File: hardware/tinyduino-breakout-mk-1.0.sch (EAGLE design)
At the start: 4 parts, among them J1 DF12-32-DP

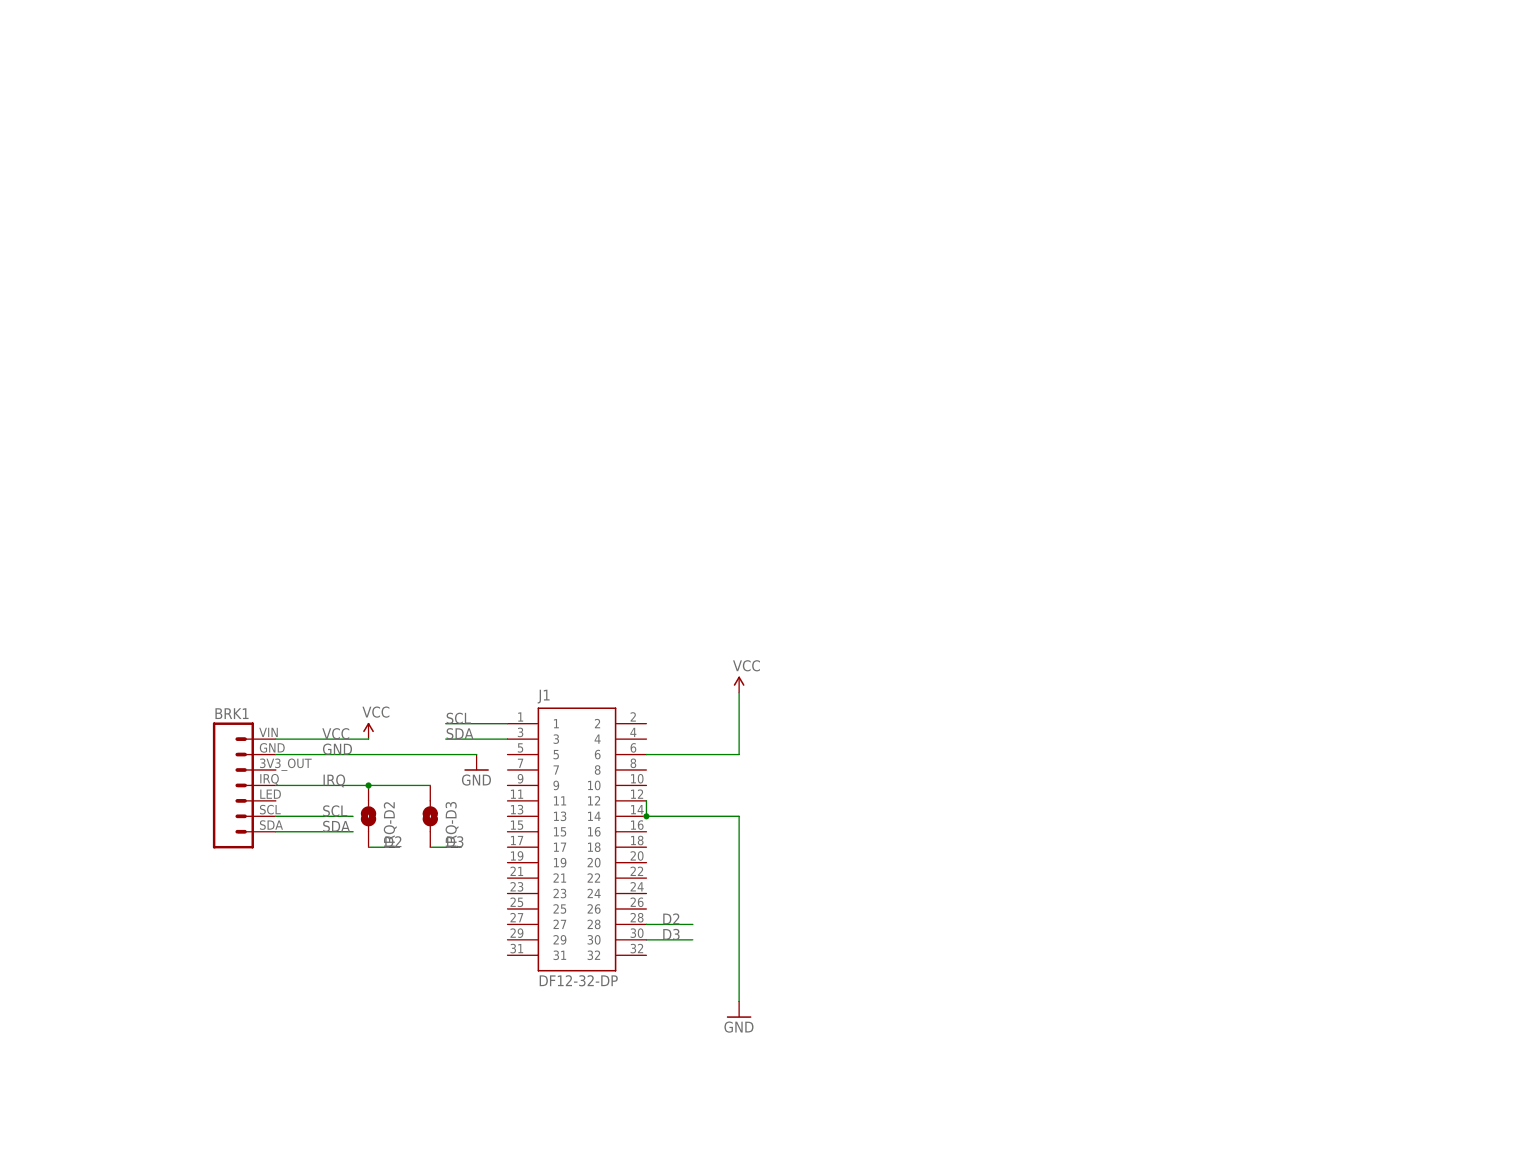
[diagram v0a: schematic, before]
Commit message: adding revsion info to schematic and board
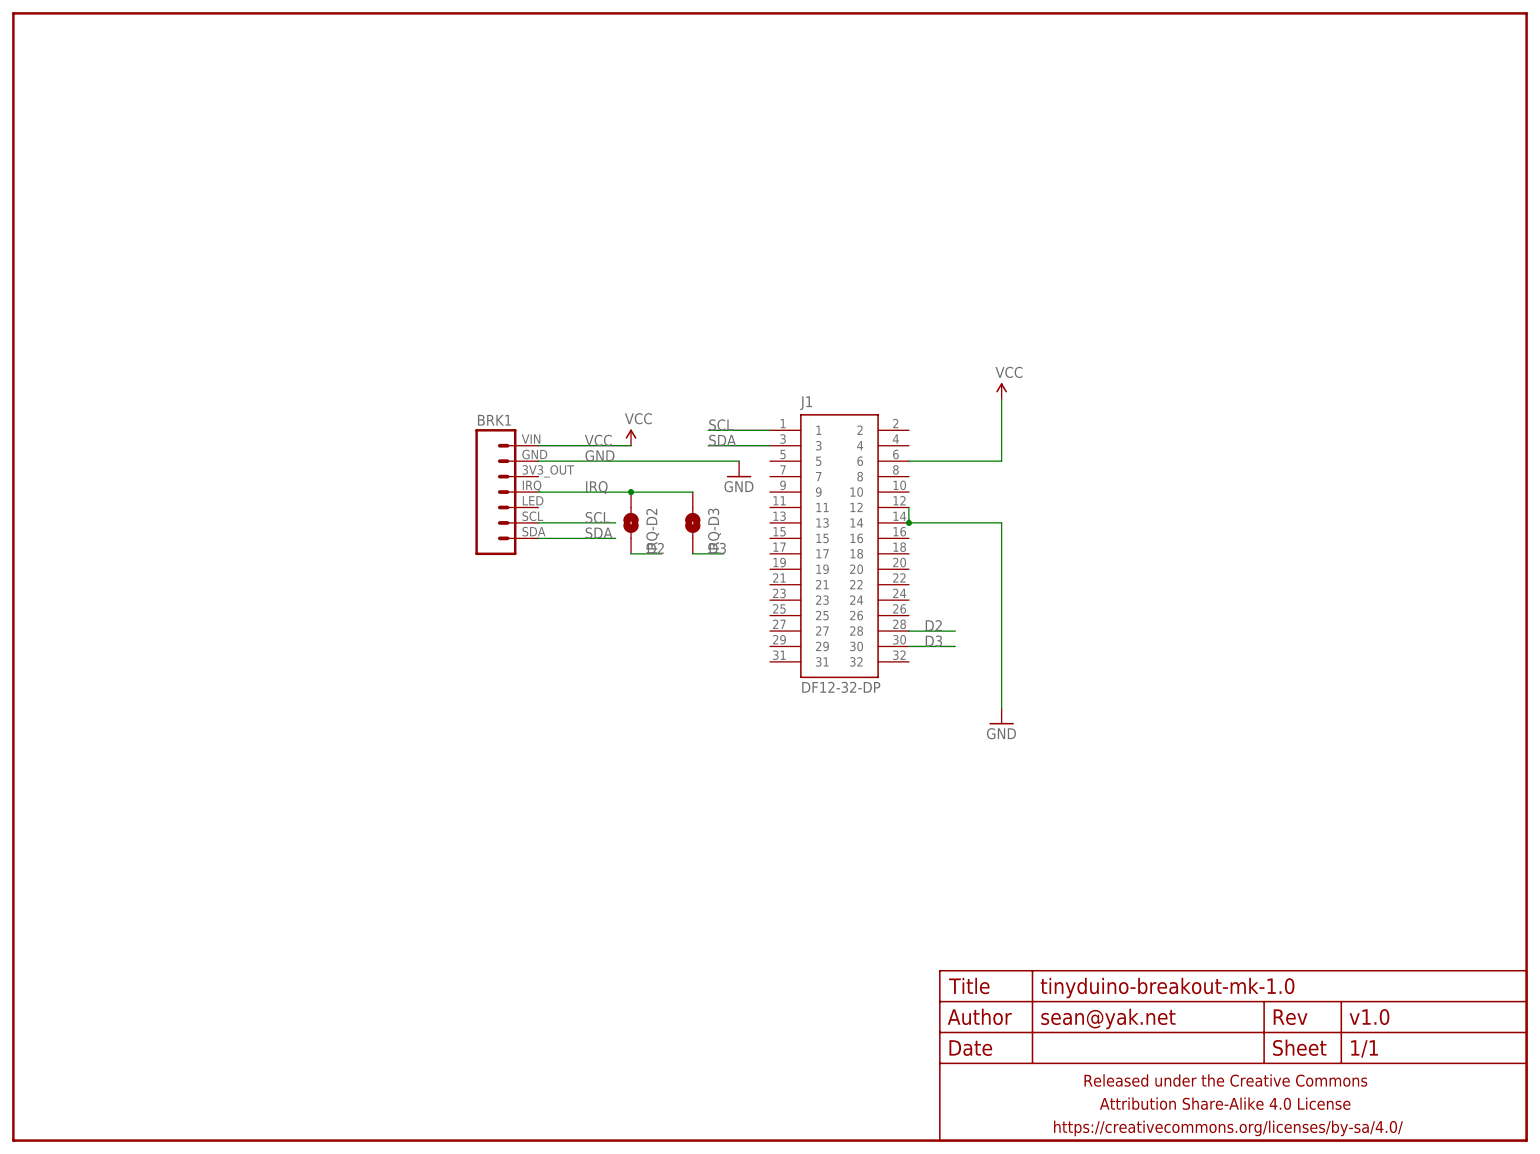
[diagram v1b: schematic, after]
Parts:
- added FRAME1: FRAME-LETTERNO_PACKAGE, A_butts:FRAME-LETTERNO_PACKAGE
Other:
- moved on the sheet: BRK1, IRQ-D2, IRQ-D3, J1
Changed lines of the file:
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@@
 <setting verticaltext="up"/>
 </settings>
-<grid distance="100" unitdist="mil" unit="mil" style="lines" multiple="1" display="yes" altdistance="1" altunitdist="mil" altunit="mil"/>
+<grid distance="100" unitdist="mil" unit="mil" style="lines" multiple="1" display="yes" altdistance="2" altunitdist="mil" altunit="mil"/>
 <layers>
 <layer number="1" name="Top" color="4" fill="1" visible="no" active="no"/>
@@
 <layer number="56" name="wert" color="7" fill="1" visible="no" active="no"/>
 <layer number="57" name="tCAD" color="7" fill="1" visible="no" active="no"/>
+<layer number="90" name="Modules" color="5" fill="1" visible="yes" active="yes"/>
 <layer number="91" name="Nets" color="2" fill="1" visible="yes" active="yes"/>
 <layer number="92" name="Busses" color="1" fill="1" visible="yes" active="yes"/>
@@
 <layer number="223" name="223bmp" color="24" fill="1" visible="yes" active="yes"/>
 <layer number="224" name="224bmp" color="25" fill="1" visible="yes" active="yes"/>
+<layer number="225" name="225bmp" color="7" fill="1" visible="yes" active="yes"/>
+<layer number="226" name="226bmp" color="7" fill="1" visible="yes" active="yes"/>
+<layer number="227" name="227bmp" color="7" fill="1" visible="yes" active="yes"/>
+<layer number="228" name="228bmp" color="7" fill="1" visible="yes" active="yes"/>
+<layer number="229" name="229bmp" color="7" fill="1" visible="yes" active="yes"/>
+<layer number="230" name="230bmp" color="7" fill="1" visible="yes" active="yes"/>
+<layer number="231" name="231bmp" color="7" fill="1" visible="yes" active="yes"/>
 <layer number="248" name="Housing" color="7" fill="1" visible="yes" active="yes"/>
 <layer number="249" name="Edge" color="7" fill="1" visible="yes" active="yes"/>
@@
 <part name="IRQ-D3" library="A_butts" deviceset="JUMPER-PAD-2-NO" device="YES_SILK"/>
 <part name="BRK1" library="A_butts" deviceset="ADAFRUIT-SI1145-BREAKOUT" device=""/>
+<part name="FRAME1" library="A_butts" deviceset="FRAME-LETTER" device="NO_PACKAGE">
+<attribute name="DESIGNER" value="sean@yak.net"/>
+<attribute name="VERSION" value="v1.0"/>
+</part>
 </parts>
 <sheets>
@@
 </plain>
 <instances>
-<instance part="J1" gate="G$1" x="91.44" y="50.8"/>
-<instance part="SUPPLY1" gate="G$1" x="58.42" y="66.04"/>
-<instance part="SUPPLY2" gate="G$1" x="119.38" y="73.66"/>
-<instance part="GND1" gate="1" x="76.2" y="60.96"/>
-<instance part="GND2" gate="1" x="119.38" y="20.32"/>
-<instance part="IRQ-D2" gate="G$1" x="58.42" y="53.34" smashed="yes" rot="R270">
-<attribute name="NAME" x="60.96" y="55.88" size="1.778" layer="95" rot="R270"/>
+<instance part="J1" gate="G$1" x="134.62" y="99.06"/>
+<instance part="SUPPLY1" gate="G$1" x="101.6" y="114.3"/>
+<instance part="SUPPLY2" gate="G$1" x="162.56" y="121.92"/>
+<instance part="GND1" gate="1" x="119.38" y="109.22"/>
+<instance part="GND2" gate="1" x="162.56" y="68.58"/>
+<instance part="IRQ-D2" gate="G$1" x="101.6" y="101.6" smashed="yes" rot="R270">
+<attribute name="NAME" x="104.14" y="104.14" size="1.778" layer="95" rot="R270"/>
 </instance>
-<instance part="IRQ-D3" gate="G$1" x="68.58" y="53.34" smashed="yes" rot="R270">
-<attribute name="NAME" x="71.12" y="55.88" size="1.778" layer="95" rot="R270"/>
+<instance part="IRQ-D3" gate="G$1" x="111.76" y="101.6" smashed="yes" rot="R270">
+<attribute name="NAME" x="114.3" y="104.14" size="1.778" layer="95" rot="R270"/>
 </instance>
-<instance part="BRK1" gate="G$1" x="38.1" y="58.42"/>
+<instance part="BRK1" gate="G$1" x="81.28" y="106.68"/>
+<instance part="FRAME1" gate="G$1" x="0" y="0"/>
+<instance part="FRAME1" gate="V" x="152.4" y="0"/>
 </instances>
 <busses>
@@
 <segment>
 <pinref part="J1" gate="G$1" pin="6"/>
-<wire x1="104.14" y1="63.5" x2="119.38" y2="63.5" width="0.1524" layer="91"/>
-<wire x1="119.38" y1="63.5" x2="119.38" y2="73.66" width="0.1524" layer="91"/>
+<wire x1="147.32" y1="111.76" x2="162.56" y2="111.76" width="0.1524" layer="91"/>
+<wire x1="162.56" y1="111.76" x2="162.56" y2="121.92" width="0.1524" layer="91"/>
 <pinref part="SUPPLY2" gate="G$1" pin="VCC"/>
 </segment>
 <segment>
-<wire x1="58.42" y1="66.04" x2="43.18" y2="66.04" width="0.1524" layer="91"/>
-<label x="50.8" y="66.04" size="1.778" layer="95"/>
+<wire x1="101.6" y1="114.3" x2="86.36" y2="114.3" width="0.1524" layer="91"/>
+<label x="93.98" y="114.3" size="1.778" layer="95"/>
 <pinref part="SUPPLY1" gate="G$1" pin="VCC"/>
 <pinref part="BRK1" gate="G$1" pin="VIN"/>
@@
 <pinref part="J1" gate="G$1" pin="12"/>
 <pinref part="J1" gate="G$1" pin="14"/>
-<wire x1="104.14" y1="55.88" x2="104.14" y2="53.34" width="0.1524" layer="91"/>
-<wire x1="104.14" y1="53.34" x2="119.38" y2="53.34" width="0.1524" layer="91"/>
-<junction x="104.14" y="53.34"/>
-<wire x1="119.38" y1="53.34" x2="119.38" y2="22.86" width="0.1524" layer="91"/>
+<wire x1="147.32" y1="104.14" x2="147.32" y2="101.6" width="0.1524" layer="91"/>
+<wire x1="147.32" y1="101.6" x2="162.56" y2="101.6" width="0.1524" layer="91"/>
+<junction x="147.32" y="101.6"/>
+<wire x1="162.56" y1="101.6" x2="162.56" y2="71.12" width="0.1524" layer="91"/>
 <pinref part="GND2" gate="1" pin="GND"/>
 </segment>
 <segment>
-<wire x1="76.2" y1="63.5" x2="43.18" y2="63.5" width="0.1524" layer="91"/>
-<label x="50.8" y="63.5" size="1.778" layer="95"/>
+<wire x1="119.38" y1="111.76" x2="86.36" y2="111.76" width="0.1524" layer="91"/>
+<label x="93.98" y="111.76" size="1.778" layer="95"/>
 <pinref part="GND1" gate="1" pin="GND"/>
 <pinref part="BRK1" gate="G$1" pin="GND"/>
@@
 <net name="IRQ" class="0">
 <segment>
-<wire x1="58.42" y1="58.42" x2="43.18" y2="58.42" width="0.1524" layer="91"/>
-<label x="50.8" y="58.42" size="1.778" layer="95"/>
+<wire x1="101.6" y1="106.68" x2="86.36" y2="106.68" width="0.1524" layer="91"/>
+<label x="93.98" y="106.68" size="1.778" layer="95"/>
 <pinref part="IRQ-D2" gate="G$1" pin="1"/>
 <pinref part="IRQ-D3" gate="G$1" pin="1"/>
-<wire x1="58.42" y1="58.42" x2="68.58" y2="58.42" width="0.1524" layer="91"/>
-<junction x="58.42" y="58.42"/>
+<wire x1="101.6" y1="106.68" x2="111.76" y2="106.68" width="0.1524" layer="91"/>
+<junction x="101.6" y="106.68"/>
 <pinref part="BRK1" gate="G$1" pin="IRQ"/>
 </segment>
@@
 <segment>
 <pinref part="J1" gate="G$1" pin="1"/>
-<wire x1="81.28" y1="68.58" x2="71.12" y2="68.58" width="0.1524" layer="91"/>
-<label x="71.12" y="68.58" size="1.778" layer="95"/>
-</segment>
-<segment>
-<wire x1="55.88" y1="53.34" x2="43.18" y2="53.34" width="0.1524" layer="91"/>
-<label x="50.8" y="53.34" size="1.778" layer="95"/>
+<wire x1="124.46" y1="116.84" x2="114.3" y2="116.84" width="0.1524" layer="91"/>
+<label x="114.3" y="116.84" size="1.778" layer="95"/>
+</segment>
+<segment>
+<wire x1="99.06" y1="101.6" x2="86.36" y2="101.6" width="0.1524" layer="91"/>
+<label x="93.98" y="101.6" size="1.778" layer="95"/>
 <pinref part="BRK1" gate="G$1" pin="SCL"/>
 </segment>
@@
 <segment>
 <pinref part="J1" gate="G$1" pin="3"/>
-<wire x1="81.28" y1="66.04" x2="71.12" y2="66.04" width="0.1524" layer="91"/>
-<label x="71.12" y="66.04" size="1.778" layer="95"/>
-</segment>
-<segment>
-<wire x1="55.88" y1="50.8" x2="43.18" y2="50.8" width="0.1524" layer="91"/>
-<label x="50.8" y="50.8" size="1.778" layer="95"/>
+<wire x1="124.46" y1="114.3" x2="114.3" y2="114.3" width="0.1524" layer="91"/>
+<label x="114.3" y="114.3" size="1.778" layer="95"/>
+</segment>
+<segment>
+<wire x1="99.06" y1="99.06" x2="86.36" y2="99.06" width="0.1524" layer="91"/>
+<label x="93.98" y="99.06" size="1.778" layer="95"/>
 <pinref part="BRK1" gate="G$1" pin="SDA"/>
 </segment>
@@
 <segment>
 <pinref part="J1" gate="G$1" pin="28"/>
-<wire x1="104.14" y1="35.56" x2="111.76" y2="35.56" width="0.1524" layer="91"/>
-<label x="106.68" y="35.56" size="1.778" layer="95"/>
+<wire x1="147.32" y1="83.82" x2="154.94" y2="83.82" width="0.1524" layer="91"/>
+<label x="149.86" y="83.82" size="1.778" layer="95"/>
 </segment>
 <segment>
 <pinref part="IRQ-D2" gate="G$1" pin="2"/>
-<wire x1="58.42" y1="48.26" x2="63.5" y2="48.26" width="0.1524" layer="91"/>
-<label x="60.96" y="48.26" size="1.778" layer="95"/>
+<wire x1="101.6" y1="96.52" x2="106.68" y2="96.52" width="0.1524" layer="91"/>
+<label x="104.14" y="96.52" size="1.778" layer="95"/>
 </segment>
 </net>
@@
 <segment>
 <pinref part="J1" gate="G$1" pin="30"/>
-<wire x1="104.14" y1="33.02" x2="111.76" y2="33.02" width="0.1524" layer="91"/>
-<label x="106.68" y="33.02" size="1.778" layer="95"/>
+<wire x1="147.32" y1="81.28" x2="154.94" y2="81.28" width="0.1524" layer="91"/>
+<label x="149.86" y="81.28" size="1.778" layer="95"/>
 </segment>
 <segment>
 <pinref part="IRQ-D3" gate="G$1" pin="2"/>
-<wire x1="68.58" y1="48.26" x2="73.66" y2="48.26" width="0.1524" layer="91"/>
-<label x="71.12" y="48.26" size="1.778" layer="95"/>
-</segment>
-</net>
+<wire x1="111.76" y1="96.52" x2="116.84" y2="96.52" width="0.1524" layer="91"/>
+<label x="114.3" y="96.52" size="1.778" layer="95"/>
+</segment>
+</net>
